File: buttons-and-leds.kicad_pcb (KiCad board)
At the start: 2 copper layers, 81.3 x 31.8 mm, 19 parts, among them P1 CONN_02X09, SW1 SW_Push, SW2 SW_Push, SW3 SW_Push, SW4 SW_Push, SW5 SW_Push, SW6 SW_Push, SW7 SW_Push, SW8 SW_Push

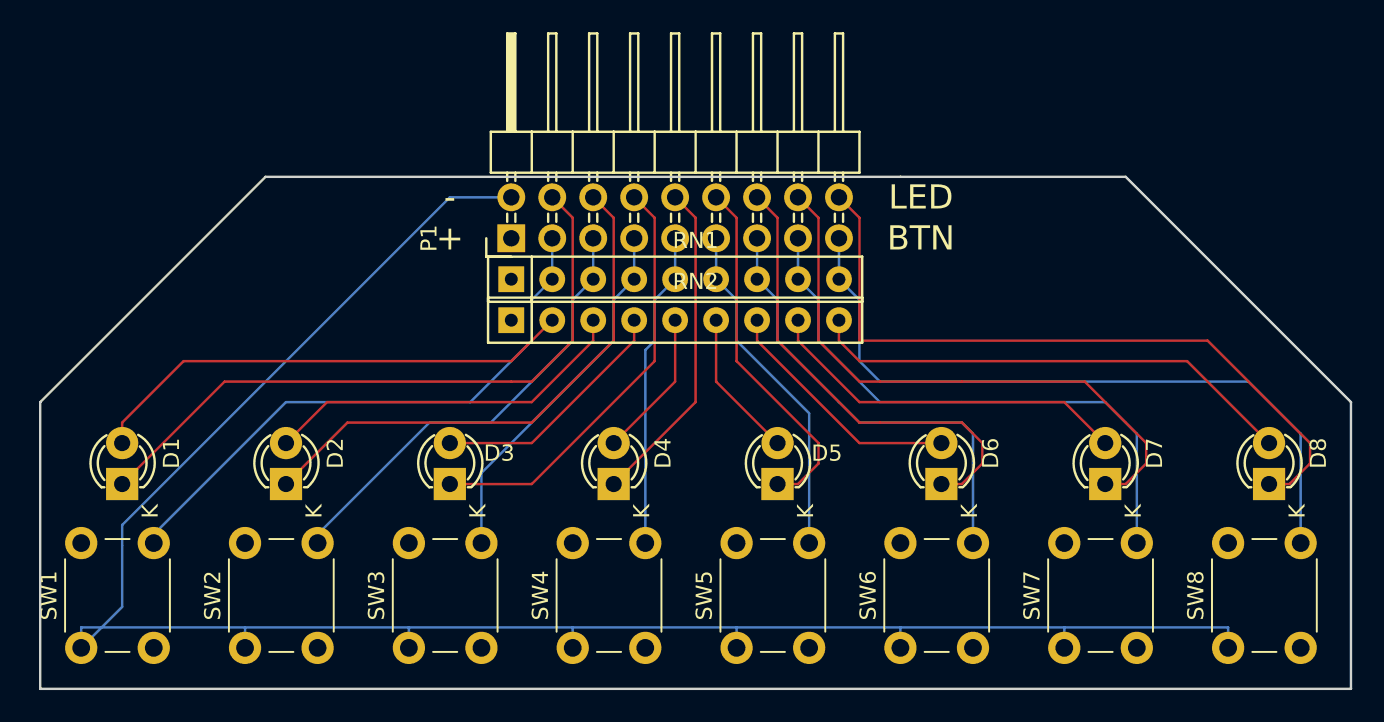
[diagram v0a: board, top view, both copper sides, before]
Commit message: Smaller and prettier
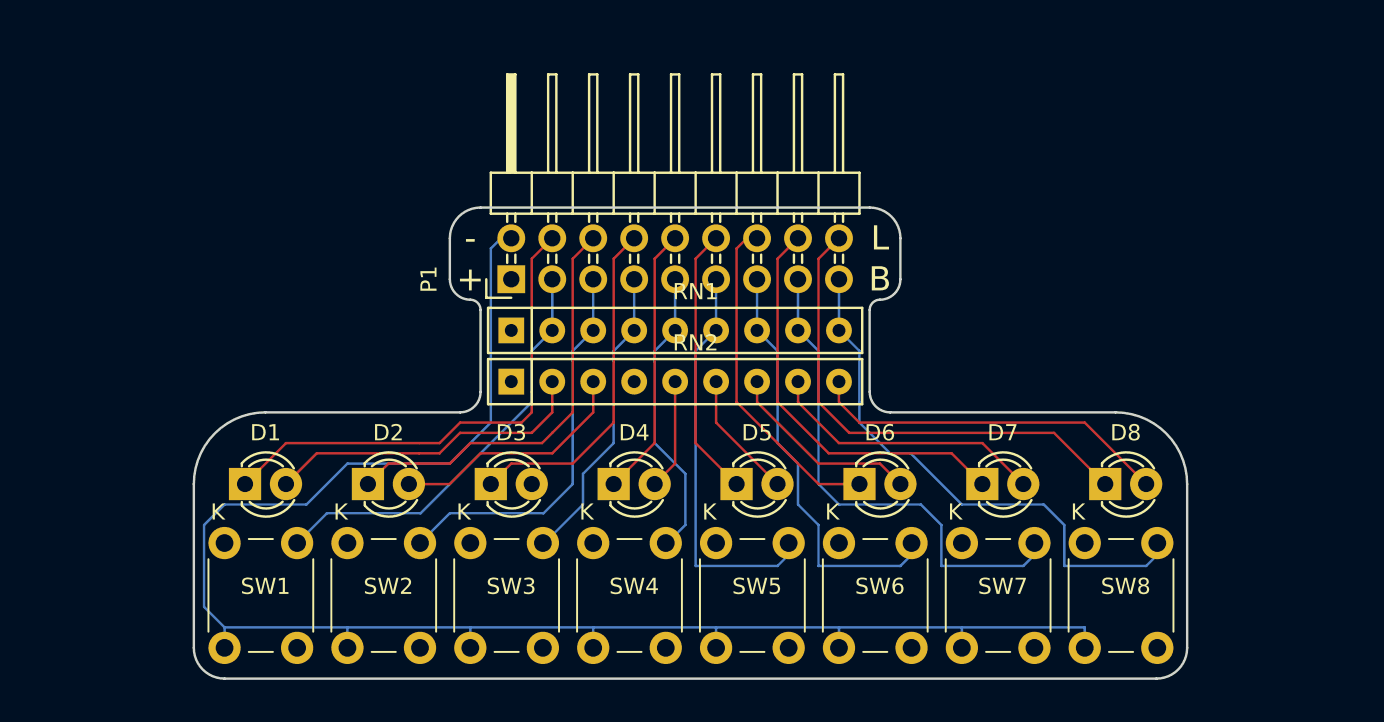
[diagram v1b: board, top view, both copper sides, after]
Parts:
- moved D8 10.2 mm to (231.1, 118.1), turned to 0 degrees
- moved SW1 8.89 mm to (176.5, 128.3)
- moved SW8 8.89 mm to (229.9, 128.3)
- moved D1 7.62 mm to (177.8, 118.1), turned to 0 degrees
- moved D7 7.62 mm to (223.5, 118.1), turned to 0 degrees
- moved SW2 6.35 mm to (184.2, 128.3)
- moved SW7 6.35 mm to (222.2, 128.3)
- moved D2 5.08 mm to (185.4, 118.1), turned to 0 degrees
- moved D6 5.08 mm to (215.9, 118.1), turned to 0 degrees
- moved RN2 3.81 mm to (194.3, 111.8)
- moved SW3 3.81 mm to (191.8, 128.3)
- moved SW6 3.81 mm to (214.6, 128.3)
- moved RN1 3.17 mm to (194.3, 108.6)
- moved D3 2.54 mm to (193.0, 118.1), turned to 0 degrees
- moved D5 2.54 mm to (208.3, 118.1), turned to 0 degrees
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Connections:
- P1 pad 1: GND -> VCC
- P1 pad 2: VCC -> GND
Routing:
- net VCC: track 33.8 -> 0.00 mm
- net Net-(D3-Pad2): track 15.3 -> 0.00 mm
- net GND: track 88.7 -> 103.9 mm
- net Net-(D8-Pad1): track 44.3 -> 31.2 mm
- net Net-(D7-Pad1): track 36.7 -> 26.1 mm
- net Net-(D1-Pad2): track 30.6 -> 20.3 mm
- net Net-(P1-Pad17): track 44.2 -> 34.1 mm
- net Net-(P1-Pad3): track 35.8 -> 26.3 mm
- net Net-(D1-Pad1): track 41.0 -> 31.6 mm
- net Net-(D6-Pad1): track 29.1 -> 21.0 mm
- net Net-(D2-Pad2): track 23.0 -> 15.2 mm
- net Net-(D8-Pad2): track 30.6 -> 23.1 mm
- net Net-(D2-Pad1): track 33.4 -> 26.5 mm
- net Net-(D7-Pad2): track 23.0 -> 18.0 mm
- net Net-(D5-Pad1): track 22.2 -> 17.5 mm
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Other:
- board size 81.3 x 31.8 mm -> 61.6 x 29.2 mm
- board text added: "B"
- board text added: "L"
- board text removed: "BTN"
- board text removed: "LED"

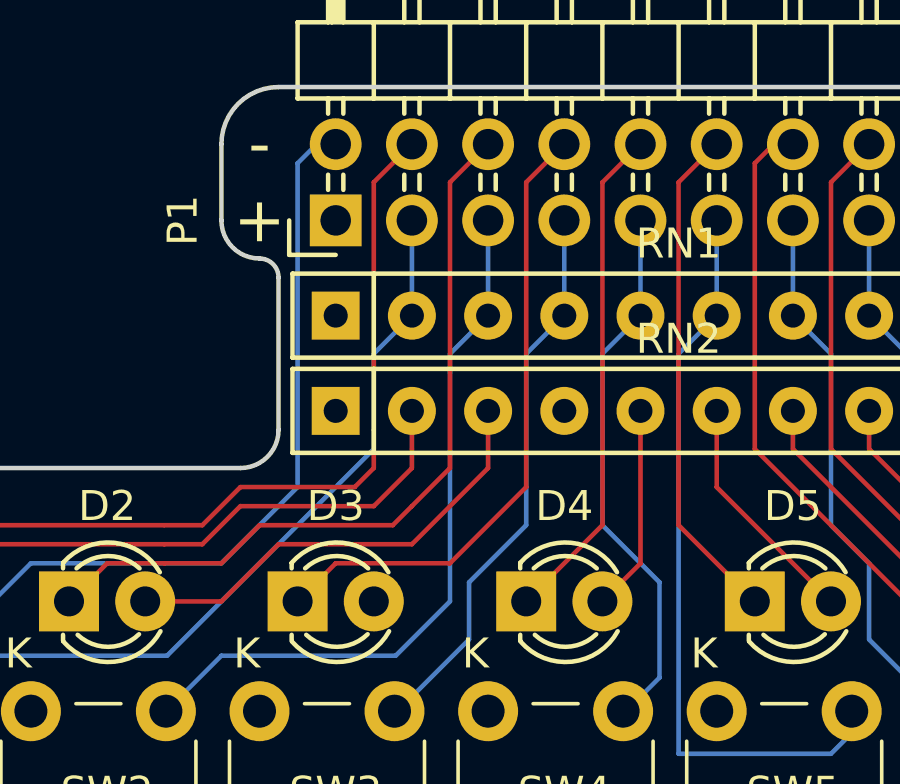
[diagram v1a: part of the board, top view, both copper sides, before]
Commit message: Oops... There are a few Missing wires!
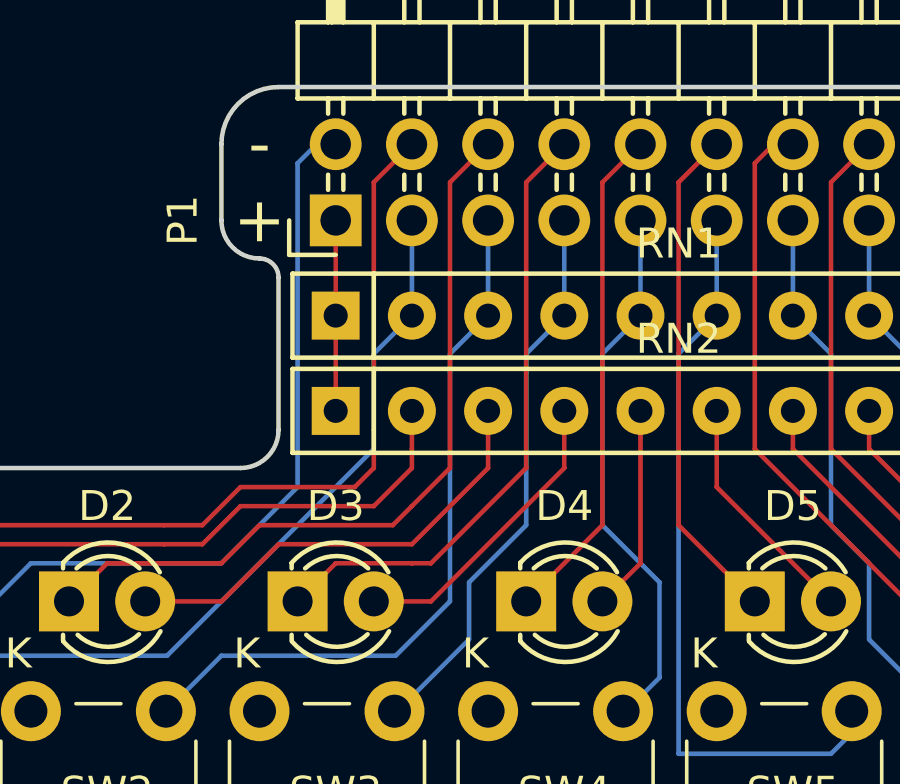
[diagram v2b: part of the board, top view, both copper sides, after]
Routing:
- net Net-(D3-Pad2): track 0.00 -> 10.1 mm
- net VCC: track 0.00 -> 6.35 mm
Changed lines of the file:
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@@
   (general
     (links 58)
-    (no_connects 19)
+    (no_connects 16)
     (area 174.549999 92.032599 237.5974 130.250001)
     (thickness 1.6)
     (drawings 26)
-    (tracks 180)
+    (tracks 186)
     (zones 0)
     (modules 19)
@@
   (segment (start 195.58 104.14) (end 195.58 112.395) (width 0.1524) (layer F.Cu) (net 1))
   (segment (start 180.34 115.57) (end 177.8 118.11) (width 0.1524) (layer F.Cu) (net 1) (status 20))
+  (segment (start 194.31 111.76) (end 194.31 108.585) (width 0.1524) (layer F.Cu) (net 2))
+  (segment (start 194.31 105.41) (end 194.31 108.585) (width 0.1524) (layer F.Cu) (net 2))
   (segment (start 196.85 114.935) (end 196.215 115.57) (width 0.1524) (layer F.Cu) (net 3))
   (segment (start 190.5 116.84) (end 188.595 116.84) (width 0.1524) (layer F.Cu) (net 3))
@@
   (segment (start 198.12 113.665) (end 196.85 114.935) (width 0.1524) (layer F.Cu) (net 3))
   (segment (start 199.39 102.235) (end 199.39 102.87) (width 0.1524) (layer F.Cu) (net 3) (status 30))
+  (segment (start 197.485 116.84) (end 200.66 113.665) (width 0.1524) (layer F.Cu) (net 4))
+  (segment (start 196.85 116.84) (end 197.485 116.84) (width 0.1524) (layer F.Cu) (net 4))
+  (segment (start 200.66 113.665) (end 200.66 104.14) (width 0.1524) (layer F.Cu) (net 4))
   (segment (start 201.93 102.235) (end 201.93 102.87) (width 0.1524) (layer F.Cu) (net 4) (status 30))
   (segment (start 201.93 102.87) (end 200.66 104.14) (width 0.1524) (layer F.Cu) (net 4) (status 10))
   (segment (start 193.04 118.11) (end 194.31 116.84) (width 0.1524) (layer F.Cu) (net 4) (status 10))
-  (segment (start 198.12 116.84) (end 200.66 114.3) (width 0.1524) (layer F.Cu) (net 4))
-  (segment (start 194.31 116.84) (end 198.12 116.84) (width 0.1524) (layer F.Cu) (net 4))
-  (segment (start 200.66 114.3) (end 200.66 104.14) (width 0.1524) (layer F.Cu) (net 4))
+  (segment (start 194.31 116.84) (end 196.85 116.84) (width 0.1524) (layer F.Cu) (net 4))
   (segment (start 204.47 102.235) (end 204.47 102.87) (width 0.1524) (layer F.Cu) (net 5) (status 30))
   (segment (start 204.47 102.87) (end 203.2 104.14) (width 0.1524) (layer F.Cu) (net 5) (status 10))
@@
   (segment (start 196.85 116.205) (end 192.405 116.205) (width 0.1524) (layer F.Cu) (net 20))
   (segment (start 199.39 113.665) (end 196.85 116.205) (width 0.1524) (layer F.Cu) (net 20))
+  (segment (start 197.485 118.11) (end 195.58 118.11) (width 0.1524) (layer F.Cu) (net 21))
+  (segment (start 201.93 113.665) (end 197.485 118.11) (width 0.1524) (layer F.Cu) (net 21))
+  (segment (start 201.93 111.76) (end 201.93 113.665) (width 0.1524) (layer F.Cu) (net 21))
   (segment (start 204.47 111.76) (end 204.47 116.84) (width 0.1524) (layer F.Cu) (net 22))
   (segment (start 204.47 116.84) (end 203.2 118.11) (width 0.1524) (layer F.Cu) (net 22))
